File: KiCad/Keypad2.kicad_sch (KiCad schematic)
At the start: 22 parts, among them J1 Keypad, J2 USB-C, U1 ESP32-PICO-MINI-02, U2 SP3485, U3 FT231XQ, U4 LMR16006+FB

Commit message: Keypad2
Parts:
- removed C1: 0.1uF, RevK:C_0603, symbol Device:C
- removed D2: D, Diode_SMD:D_1206_3216Metric_Pad1.42x1.75mm_HandSolder, symbol Device:D
- removed J2: USB-C, RevK:USC16-TR-Round, symbol Connector:USB_C_Receptacle_USB2.0
- removed R2, R3: 5K1, RevK:R_0603, symbol Device:R
- removed U3: FT231XQ, RevK:QFN-20-1EP_4x4mm_P0.5mm_EP2.5x2.5mm, symbol Interface_USB:FT231XQ
- added J2: Prog, Connector_PinHeader_2.54mm:PinHeader_1x05_P2.54mm_Vertical, symbol Connector_Generic:Conn_01x05
- renumbered C2 to C1, C3 to C2, C4 to C3, D3 to D2, R6 to R1, R7 to R2, R8 to R3, R9 to R4, R10 to R5, U2 to U1, U1 to U2, U4 to U3
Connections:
- net +3V3: now also J2.3 (Pin_3)
- net B: now also U2.17 (IO27); no longer U2.24 (IO4)
- net DE: now also U2.19 (IO12); no longer U2.15 (IO25)
- net G: now also U2.16 (IO26); no longer U2.34 (IO22)
- net GND: now also J2.1 (Pin_1)
- net I: now also J2.5 (Pin_5)
- net O: now also J2.4 (Pin_4)
- net R: now also U2.15 (IO25); no longer U2.35 (IO21)
- net RX: now also U2.20 (IO13); no longer U2.16 (IO26)
- net TX: now also U2.18 (IO14)
- net BOOT renamed GPIO0
- net GPIO0: now also J2.2 (Pin_2)
- no-connect marks 6 -> 0
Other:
- moved on the sheet: J1, U1, U2

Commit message: Checking
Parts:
- U1: footprint Package_SO:SOIC-8_3.9x4.9mm_P1.27mm -> Package_SO:SO-8_3.9x4.9mm_P1.27mm
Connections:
- net EN is gone; now on net +3V3: U2.8 (EN)
- no-connect marks 0 -> 18
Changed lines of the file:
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@@
   (junction (at 233.68 33.02) (diameter 0) (color 0 0 0 0)
   )
-  (wire (pts (xy 97.79 41.91) (xy 102.87 41.91))
-    (stroke (width 0) (type default) (color 0 0 0 0))
-  )
+  (no_connect (at 133.35 82.55))
+  (no_connect (at 133.35 80.01))
+  (no_connect (at 102.87 44.45))
+  (no_connect (at 102.87 85.09))
+  (no_connect (at 102.87 57.15))
+  (no_connect (at 102.87 64.77))
+  (no_connect (at 102.87 67.31))
+  (no_connect (at 102.87 69.85))
+  (no_connect (at 102.87 72.39))
+  (no_connect (at 102.87 74.93))
+  (no_connect (at 133.35 67.31))
+  (no_connect (at 133.35 69.85))
+  (no_connect (at 102.87 54.61))
+  (no_connect (at 102.87 46.99))
+  (no_connect (at 102.87 49.53))
+  (no_connect (at 102.87 52.07))
+  (no_connect (at 133.35 64.77))
+  (no_connect (at 133.35 62.23))
   (wire (pts (xy 81.28 121.92) (xy 81.28 142.24))
     (stroke (width 0) (type default) (color 0 0 0 0))
@@
     (property "Intersheet References" "${INTERSHEET_REFS}" (id 0) (at 115.7253 138.3506 0)
       (effects (font (size 1.27 1.27)) (justify right) hide)
-    )
-  )
-  (global_label "EN" (shape input) (at 97.79 41.91 180) (fields_autoplaced)
-    (effects (font (size 1.27 1.27)) (justify right))
-    (property "Intersheet References" "${INTERSHEET_REFS}" (id 0) (at 56.515 0 0)
-      (effects (font (size 1.27 1.27)) hide)
     )
   )
@@
     (property "Reference" "U1" (id 0) (at 50.165 129.159 0))
     (property "Value" "SP3485" (id 1) (at 50.165 131.4704 0))
-    (property "Footprint" "Package_SO:SOIC-8_3.9x4.9mm_P1.27mm" (id 2) (at 49.53 153.67 0)
+    (property "Footprint" "Package_SO:SO-8_3.9x4.9mm_P1.27mm" (id 2) (at 49.53 153.67 0)
       (effects (font (size 1.27 1.27)) hide)
     )
@@
     (pin "2")
   )
-  (symbol (lib_name "Hidden_1") (lib_id "RevK:Hidden") (at 255.905 33.655 0) (unit 1)
+  (symbol (lib_id "RevK:Hidden") (at 255.905 33.655 0) (unit 1)
     (in_bom yes) (on_board yes)
     (property "Reference" "C1" (id 0) (at 256.54 33.655 0)
@@
     (pin "~")
   )
-  (symbol (lib_name "Hidden_2") (lib_id "RevK:Hidden") (at 255.905 35.56 0) (unit 1)
+  (symbol (lib_id "RevK:Hidden") (at 255.905 35.56 0) (unit 1)
     (in_bom yes) (on_board yes)
     (property "Reference" "C2" (id 0) (at 256.54 35.56 0)
@@
     (pin "~")
   )
-  (symbol (lib_name "Hidden_3") (lib_id "RevK:Hidden") (at 255.905 37.465 0) (unit 1)
+  (symbol (lib_id "RevK:Hidden") (at 255.905 37.465 0) (unit 1)
     (in_bom yes) (on_board yes)
     (property "Reference" "C3" (id 0) (at 256.54 37.465 0)
@@
     (pin "~")
   )
-  (symbol (lib_name "Hidden_4") (lib_id "RevK:Hidden") (at 255.905 39.37 0) (unit 1)
+  (symbol (lib_id "RevK:Hidden") (at 255.905 39.37 0) (unit 1)
     (in_bom yes) (on_board yes)
     (property "Reference" "L1" (id 0) (at 256.54 39.37 0)
@@
     (pin "1")
   )
-  (symbol (lib_id "power:+3.3V") (at 101.6 41.91 0) (unit 1)
+  (symbol (lib_id "power:+3.3V") (at 102.87 41.91 90) (unit 1)
     (in_bom yes) (on_board yes) (fields_autoplaced)
-    (property "Reference" "#PWR05" (id 0) (at 101.6 45.72 0)
-      (effects (font (size 1.27 1.27)) hide)
-    )
-    (property "Value" "+3.3V" (id 1) (at 101.6 38.3342 0))
-    (property "Footprint" "" (id 2) (at 101.6 41.91 0)
-      (effects (font (size 1.27 1.27)) hide)
-    )
-    (property "Datasheet" "" (id 3) (at 101.6 41.91 0)
+    (property "Reference" "#PWR05" (id 0) (at 106.68 41.91 0)
+      (effects (font (size 1.27 1.27)) hide)
+    )
+    (property "Value" "+3.3V" (id 1) (at 99.695 42.3438 90)
+      (effects (font (size 1.27 1.27)) (justify left))
+    )
+    (property "Footprint" "" (id 2) (at 102.87 41.91 0)
+      (effects (font (size 1.27 1.27)) hide)
+    )
+    (property "Datasheet" "" (id 3) (at 102.87 41.91 0)
       (effects (font (size 1.27 1.27)) hide)
     )
@@
     )
     (path "/00000000-0000-0000-0000-000060718926"
-      (reference "U1") (unit 1) (value "SP3485") (footprint "Package_SO:SOIC-8_3.9x4.9mm_P1.27mm")
+      (reference "U1") (unit 1) (value "SP3485") (footprint "Package_SO:SO-8_3.9x4.9mm_P1.27mm")
     )
     (path "/784f2ed4-8f1b-4283-9869-b3ecce1e695e"

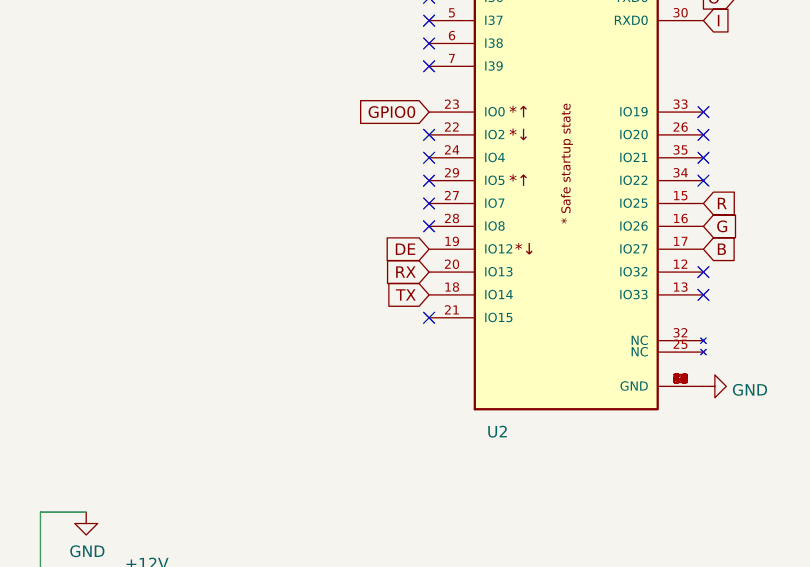
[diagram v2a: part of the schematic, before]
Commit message: Tweaked some GPIO, and added to documentation
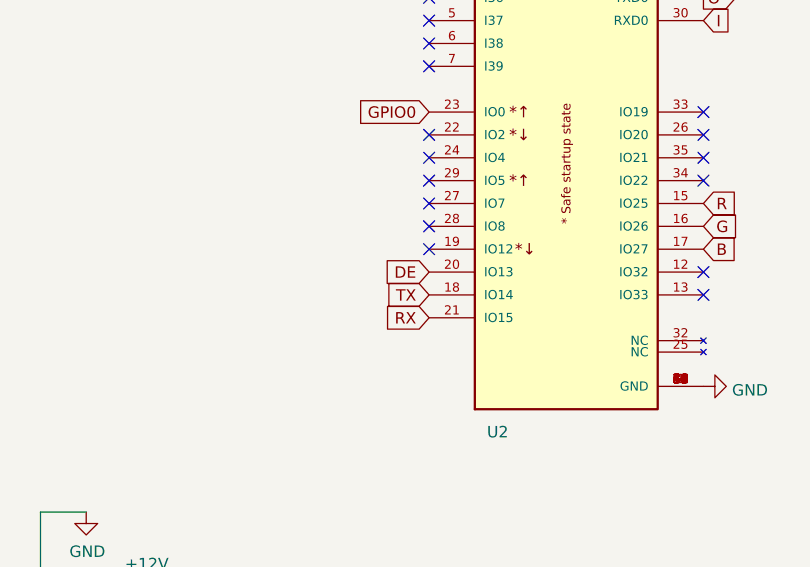
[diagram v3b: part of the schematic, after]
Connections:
- net DE: now also U2.20 (IO13); no longer U2.19 (IO12)
- net RX: now also U2.21 (IO15); no longer U2.20 (IO13)
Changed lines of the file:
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@@
   (no_connect (at 133.35 80.01))
   (no_connect (at 102.87 44.45))
-  (no_connect (at 102.87 85.09))
+  (no_connect (at 102.87 77.47))
   (no_connect (at 102.87 57.15))
   (no_connect (at 102.87 64.77))
@@
     )
   )
-  (global_label "DE" (shape input) (at 102.87 77.47 180) (fields_autoplaced)
+  (global_label "DE" (shape input) (at 102.87 80.01 180) (fields_autoplaced)
     (effects (font (size 1.27 1.27)) (justify right))
-    (property "Intersheet References" "${INTERSHEET_REFS}" (id 0) (at 187.325 137.16 0)
+    (property "Intersheet References" "${INTERSHEET_REFS}" (id 0) (at 187.325 139.7 0)
       (effects (font (size 1.27 1.27)) hide)
     )
@@
     )
   )
-  (global_label "RX" (shape input) (at 102.87 80.01 180) (fields_autoplaced)
+  (global_label "RX" (shape input) (at 102.87 85.09 180) (fields_autoplaced)
     (effects (font (size 1.27 1.27)) (justify right))
-    (property "Intersheet References" "${INTERSHEET_REFS}" (id 0) (at 187.325 170.18 0)
+    (property "Intersheet References" "${INTERSHEET_REFS}" (id 0) (at 187.325 175.26 0)
       (effects (font (size 1.27 1.27)) hide)
     )

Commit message: Clean up
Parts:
- removed Logo1: AA, RevK:AA, symbol RevK:AA
- added Logo1: AJK, RevK:AJK, symbol RevK:AJK
- added U4: QR, RevK:QR-SS, symbol RevK:QR
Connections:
- net GND: no longer U2.54 (GND), U2.55 (GND), U2.56 (GND), U2.57 (GND), U2.58 (GND), U2.59 (GND), U2.60 (GND), U2.61 (GND)
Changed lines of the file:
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@@
     (pin "1")
-  )
-  (symbol (lib_id "RevK:AA") (at 266.7 172.72 0) (unit 1)
-    (in_bom yes) (on_board yes)
-    (property "Reference" "Logo1" (id 0) (at 266.7 172.72 0)
-      (effects (font (size 1.27 1.27)) hide)
-    )
-    (property "Value" "AA" (id 1) (at 267.335 172.72 0)
-      (effects (font (size 1.27 1.27)) (justify left))
-    )
-    (property "Footprint" "RevK:AA" (id 2) (at 266.7 172.72 0)
-      (effects (font (size 1.27 1.27)) hide)
-    )
-    (property "Datasheet" "" (id 3) (at 266.7 172.72 0)
-      (effects (font (size 1.27 1.27)) hide)
-    )
-    (property "Note" "Non part, PCB printed" (id 4) (at 266.7 172.72 0)
-      (effects (font (size 1.27 1.27)) hide)
-    )
   )
   (symbol (lib_id "power:+12V") (at 71.12 116.84 0) (unit 1)
@@
     (pin "1")
   )
+  (symbol (lib_id "RevK:QR") (at 274.32 172.72 0) (unit 1)
+    (in_bom no) (on_board yes) (fields_autoplaced)
+    (property "Reference" "U4" (id 0) (at 274.32 175.895 0)
+      (effects (font (size 1.27 1.27)) hide)
+    )
+    (property "Value" "QR" (id 1) (at 274.32 175.895 0)
+      (effects (font (size 1.27 1.27)) hide)
+    )
+    (property "Footprint" "RevK:QR-SS" (id 2) (at 273.685 173.355 0)
+      (effects (font (size 1.27 1.27)) hide)
+    )
+    (property "Datasheet" "" (id 3) (at 273.685 173.355 0)
+      (effects (font (size 1.27 1.27)) hide)
+    )
+    (property "Note" "Non part, PCB printed" (id 4) (at 274.32 172.72 0)
+      (effects (font (size 1.27 1.27)) hide)
+    )
+  )
   (symbol (lib_id "power:GND") (at 240.03 50.8 0) (unit 1)
     (in_bom yes) (on_board yes) (fields_autoplaced)
@@
       (effects (font (size 1.27 1.27)) (justify left))
     )
-    (property "Footprint" "Connector_PinHeader_2.54mm:PinHeader_1x05_P2.54mm_Vertical" (id 2) (at 124.46 135.89 0)
+    (property "Footprint" "Connector_PinHeader_2.54mm:PinHeader_1x05_P2.54mm_Vertical" (id 2) (at 124.46 143.51 0)
       (effects (font (size 1.27 1.27)) hide)
     )
@@
     (pin "52")
     (pin "53")
-    (pin "54")
-    (pin "55")
-    (pin "56")
-    (pin "57")
-    (pin "58")
-    (pin "59")
     (pin "6")
-    (pin "60")
-    (pin "61")
     (pin "7")
     (pin "8")
@@
     )
     (pin "1")
+  )
+  (symbol (lib_id "RevK:AJK") (at 269.24 172.72 0) (unit 1)
+    (in_bom no) (on_board yes)
+    (property "Reference" "Logo1" (id 0) (at 269.24 170.18 0)
+      (effects (font (size 1.27 1.27)) hide)
+    )
+    (property "Value" "AJK" (id 1) (at 266.7 172.72 0)
+      (effects (font (size 1.27 1.27)) (justify left))
+    )
+    (property "Footprint" "RevK:AJK" (id 2) (at 269.24 175.26 0)
+      (effects (font (size 1.27 1.27)) hide)
+    )
+    (property "Datasheet" "" (id 3) (at 269.24 175.26 0)
+      (effects (font (size 1.27 1.27)) hide)
+    )
+    (property "Note" "Non part, PCB printed" (id 4) (at 269.24 172.72 0)
+      (effects (font (size 1.27 1.27)) hide)
+    )
   )
   (symbol (lib_id "power:+12V") (at 233.68 33.02 0) (unit 1)
@@
     (property "Reference" "J1" (id 0) (at 46.355 109.3302 0))
     (property "Value" "Keypad" (id 1) (at 46.355 111.8671 0))
-    (property "Footprint" "RevK:Molex_MiniSPOX_H4V" (id 2) (at 46.355 116.84 0)
+    (property "Footprint" "RevK:Molex_MiniSPOX_H4V" (id 2) (at 46.355 124.46 0)
       (effects (font (size 1.27 1.27)) hide)
     )
@@
       (reference "L1") (unit 1) (value "6.8uH") (footprint "RevK:Hidden")
     )
-    (path "/00000000-0000-0000-0000-000060b9351c"
-      (reference "Logo1") (unit 1) (value "AA") (footprint "RevK:AA")
+    (path "/d8b4cc04-1cc7-43a2-af9d-685210cb4548"
+      (reference "Logo1") (unit 1) (value "AJK") (footprint "RevK:AJK")
     )
     (path "/00000000-0000-0000-0000-000060ce4fe8"
@@
       (reference "U3") (unit 1) (value "LMR16006+FB") (footprint "RevK:RegulatorBlockFB")
     )
-  )
+    (path "/31b42c3f-ef68-4fb7-bba0-44bb7a0027da"
+      (reference "U4") (unit 1) (value "QR") (footprint "RevK:QR-SS")
+    )
+  )

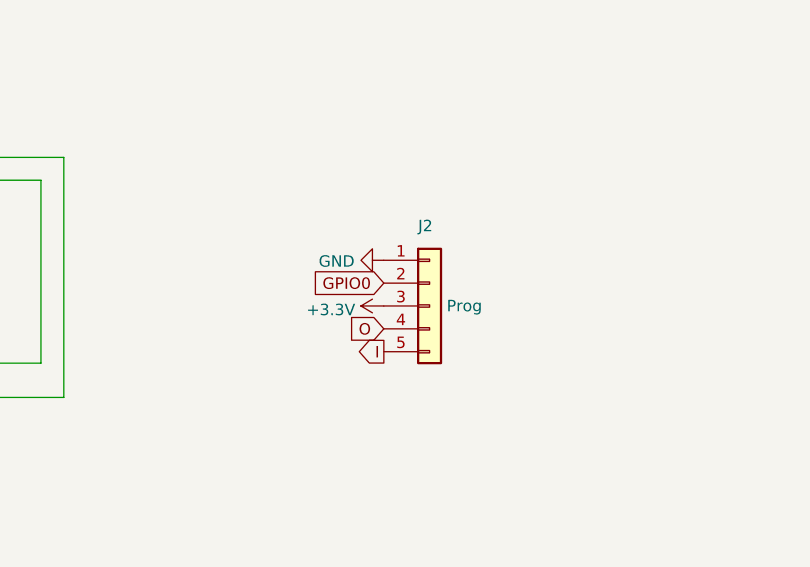
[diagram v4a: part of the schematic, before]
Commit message: Bugger, tx/rx swapped
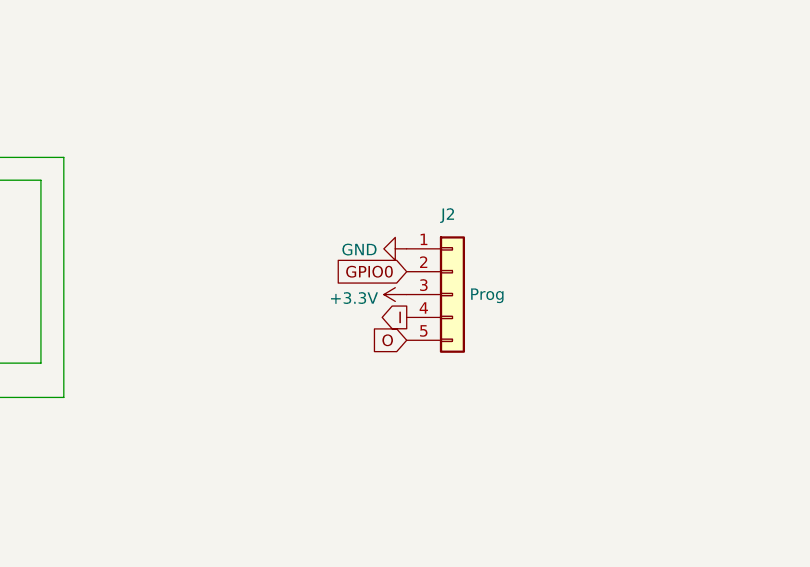
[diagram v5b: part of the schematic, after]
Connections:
- net I: now also J2.4 (Pin_4); no longer J2.5 (Pin_5)
- net O: now also J2.5 (Pin_5); no longer J2.4 (Pin_4)
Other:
- moved on the sheet: J2
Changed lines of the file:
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@@
     )
   )
-  (global_label "O" (shape input) (at 119.38 138.43 180) (fields_autoplaced)
-    (effects (font (size 1.27 1.27)) (justify right))
-    (property "Intersheet References" "${INTERSHEET_REFS}" (id 0) (at 115.7253 138.3506 0)
+  (global_label "O" (shape input) (at 121.92 139.7 180) (fields_autoplaced)
+    (effects (font (size 1.27 1.27)) (justify right))
+    (property "Intersheet References" "${INTERSHEET_REFS}" (id 0) (at 118.2653 139.6206 0)
       (effects (font (size 1.27 1.27)) (justify right) hide)
     )
@@
     )
   )
-  (global_label "I" (shape output) (at 119.38 140.97 180) (fields_autoplaced)
-    (effects (font (size 1.27 1.27)) (justify right))
-    (property "Intersheet References" "${INTERSHEET_REFS}" (id 0) (at 116.451 140.8906 0)
+  (global_label "I" (shape output) (at 121.92 137.16 180) (fields_autoplaced)
+    (effects (font (size 1.27 1.27)) (justify right))
+    (property "Intersheet References" "${INTERSHEET_REFS}" (id 0) (at 118.991 137.0806 0)
       (effects (font (size 1.27 1.27)) (justify right) hide)
     )
@@
     )
   )
-  (global_label "GPIO0" (shape input) (at 119.38 133.35 180) (fields_autoplaced)
-    (effects (font (size 1.27 1.27)) (justify right))
-    (property "Intersheet References" "${INTERSHEET_REFS}" (id 0) (at 50.8 92.71 0)
+  (global_label "GPIO0" (shape input) (at 121.92 132.08 180) (fields_autoplaced)
+    (effects (font (size 1.27 1.27)) (justify right))
+    (property "Intersheet References" "${INTERSHEET_REFS}" (id 0) (at 53.34 91.44 0)
       (effects (font (size 1.27 1.27)) hide)
     )
@@
     (pin "5")
   )
-  (symbol (lib_id "power:GND") (at 119.38 130.81 270) (unit 1)
-    (in_bom yes) (on_board yes)
-    (property "Reference" "#PWR06" (id 0) (at 113.03 130.81 0)
-      (effects (font (size 1.27 1.27)) hide)
-    )
-    (property "Value" "GND" (id 1) (at 116.1288 130.937 90)
+  (symbol (lib_id "power:GND") (at 121.92 129.54 270) (unit 1)
+    (in_bom yes) (on_board yes)
+    (property "Reference" "#PWR06" (id 0) (at 115.57 129.54 0)
+      (effects (font (size 1.27 1.27)) hide)
+    )
+    (property "Value" "GND" (id 1) (at 118.6688 129.667 90)
       (effects (font (size 1.27 1.27)) (justify right))
     )
-    (property "Footprint" "" (id 2) (at 119.38 130.81 0)
-      (effects (font (size 1.27 1.27)) hide)
-    )
-    (property "Datasheet" "" (id 3) (at 119.38 130.81 0)
+    (property "Footprint" "" (id 2) (at 121.92 129.54 0)
+      (effects (font (size 1.27 1.27)) hide)
+    )
+    (property "Datasheet" "" (id 3) (at 121.92 129.54 0)
       (effects (font (size 1.27 1.27)) hide)
     )
@@
     (pin "1")
   )
-  (symbol (lib_id "Connector_Generic:Conn_01x05") (at 124.46 135.89 0) (unit 1)
+  (symbol (lib_id "Connector_Generic:Conn_01x05") (at 127 134.62 0) (unit 1)
     (in_bom no) (on_board yes)
-    (property "Reference" "J2" (id 0) (at 123.19 127 0)
-      (effects (font (size 1.27 1.27)) (justify left))
-    )
-    (property "Value" "Prog" (id 1) (at 126.365 135.89 0)
-      (effects (font (size 1.27 1.27)) (justify left))
-    )
-    (property "Footprint" "Connector_PinHeader_2.54mm:PinHeader_1x05_P2.54mm_Vertical" (id 2) (at 124.46 143.51 0)
-      (effects (font (size 1.27 1.27)) hide)
-    )
-    (property "Datasheet" "~" (id 3) (at 124.46 135.89 0)
+    (property "Reference" "J2" (id 0) (at 125.73 125.73 0)
+      (effects (font (size 1.27 1.27)) (justify left))
+    )
+    (property "Value" "Prog" (id 1) (at 128.905 134.62 0)
+      (effects (font (size 1.27 1.27)) (justify left))
+    )
+    (property "Footprint" "Connector_PinHeader_2.54mm:PinHeader_1x05_P2.54mm_Vertical" (id 2) (at 127 142.24 0)
+      (effects (font (size 1.27 1.27)) hide)
+    )
+    (property "Datasheet" "~" (id 3) (at 127 134.62 0)
       (effects (font (size 1.27 1.27)) hide)
     )
@@
     (pin "1")
   )
-  (symbol (lib_id "power:+3.3V") (at 119.38 135.89 90) (unit 1)
+  (symbol (lib_id "power:+3.3V") (at 121.92 134.62 90) (unit 1)
     (in_bom yes) (on_board yes) (fields_autoplaced)
-    (property "Reference" "#PWR07" (id 0) (at 123.19 135.89 0)
-      (effects (font (size 1.27 1.27)) hide)
-    )
-    (property "Value" "+3.3V" (id 1) (at 116.205 136.3238 90)
-      (effects (font (size 1.27 1.27)) (justify left))
-    )
-    (property "Footprint" "" (id 2) (at 119.38 135.89 0)
-      (effects (font (size 1.27 1.27)) hide)
-    )
-    (property "Datasheet" "" (id 3) (at 119.38 135.89 0)
-      (effects (font (size 1.27 1.27)) hide)
-    )
+    (property "Reference" "#PWR07" (id 0) (at 125.73 134.62 0)
+      (effects (font (size 1.27 1.27)) hide)
+    )
+    (property "Value" "+3.3V" (id 1) (at 118.745 135.0538 90)
+      (effects (font (size 1.27 1.27)) (justify left))
+    )
+    (property "Footprint" "" (id 2) (at 121.92 134.62 0)
+      (effects (font (size 1.27 1.27)) hide)
+    )
+    (property "Datasheet" "" (id 3) (at 121.92 134.62 0)
+      (effects (font (size 1.27 1.27)) hide)
+    )
